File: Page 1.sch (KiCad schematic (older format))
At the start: 36 parts, among them J1 10118192-0001LF, J2 ARJM11A3, U1 AZ1117-3.3, U2 LAN8720A

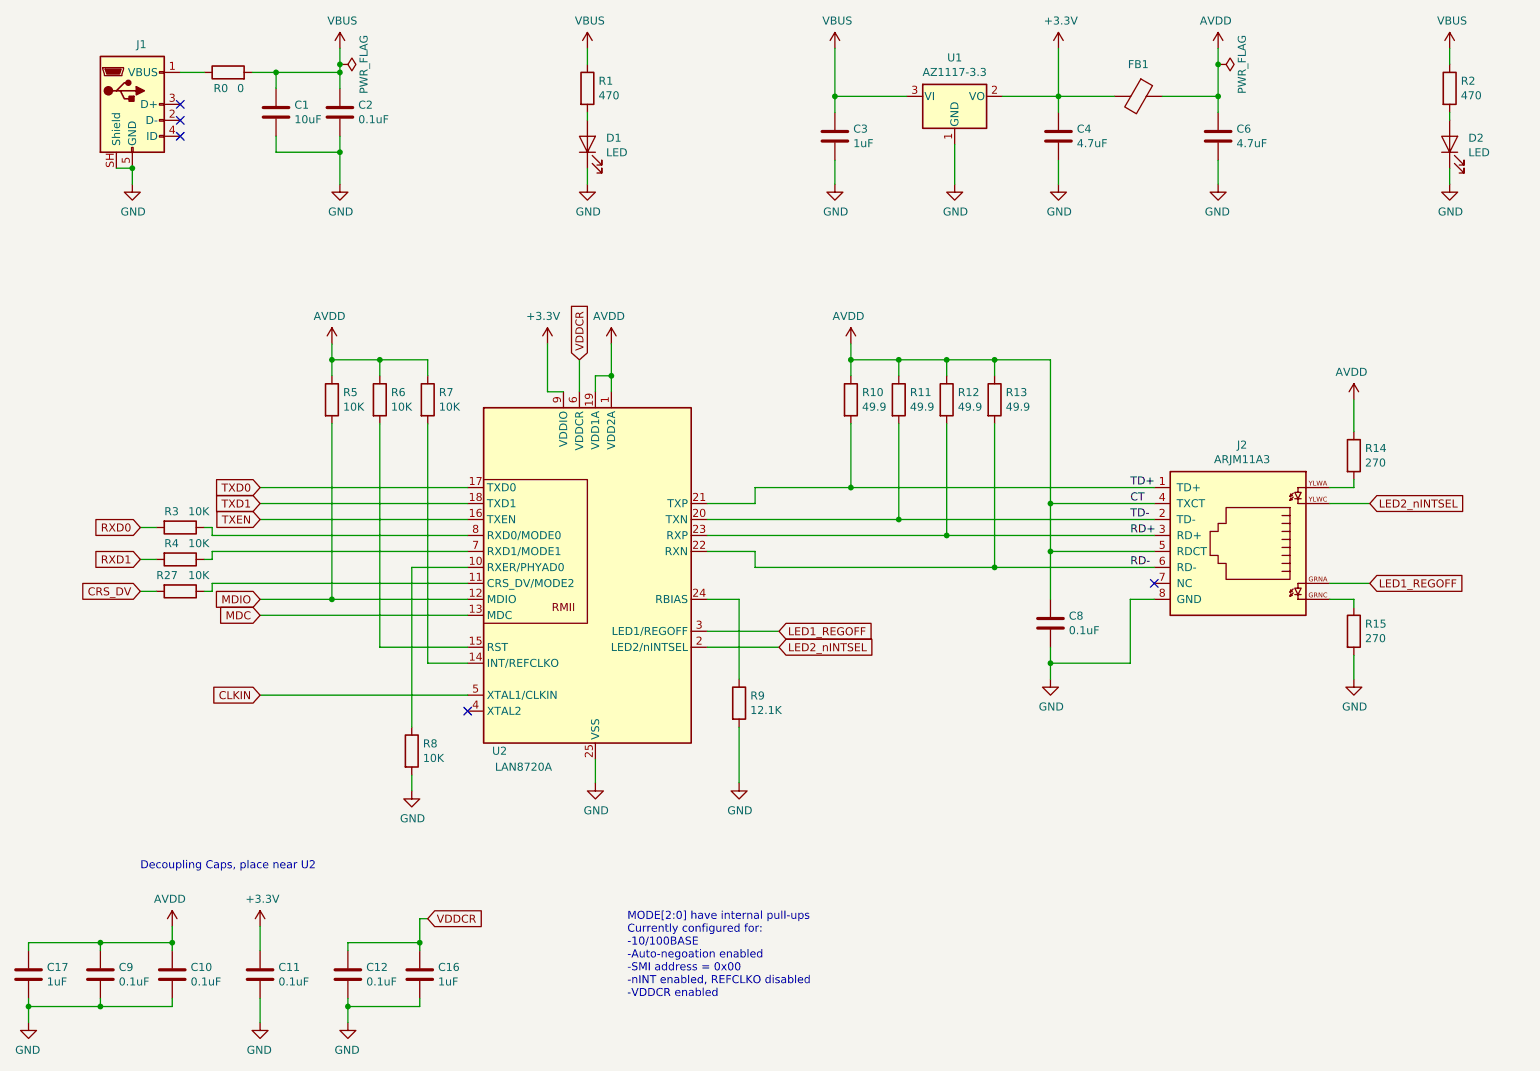
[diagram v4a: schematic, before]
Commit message: Schematic changes
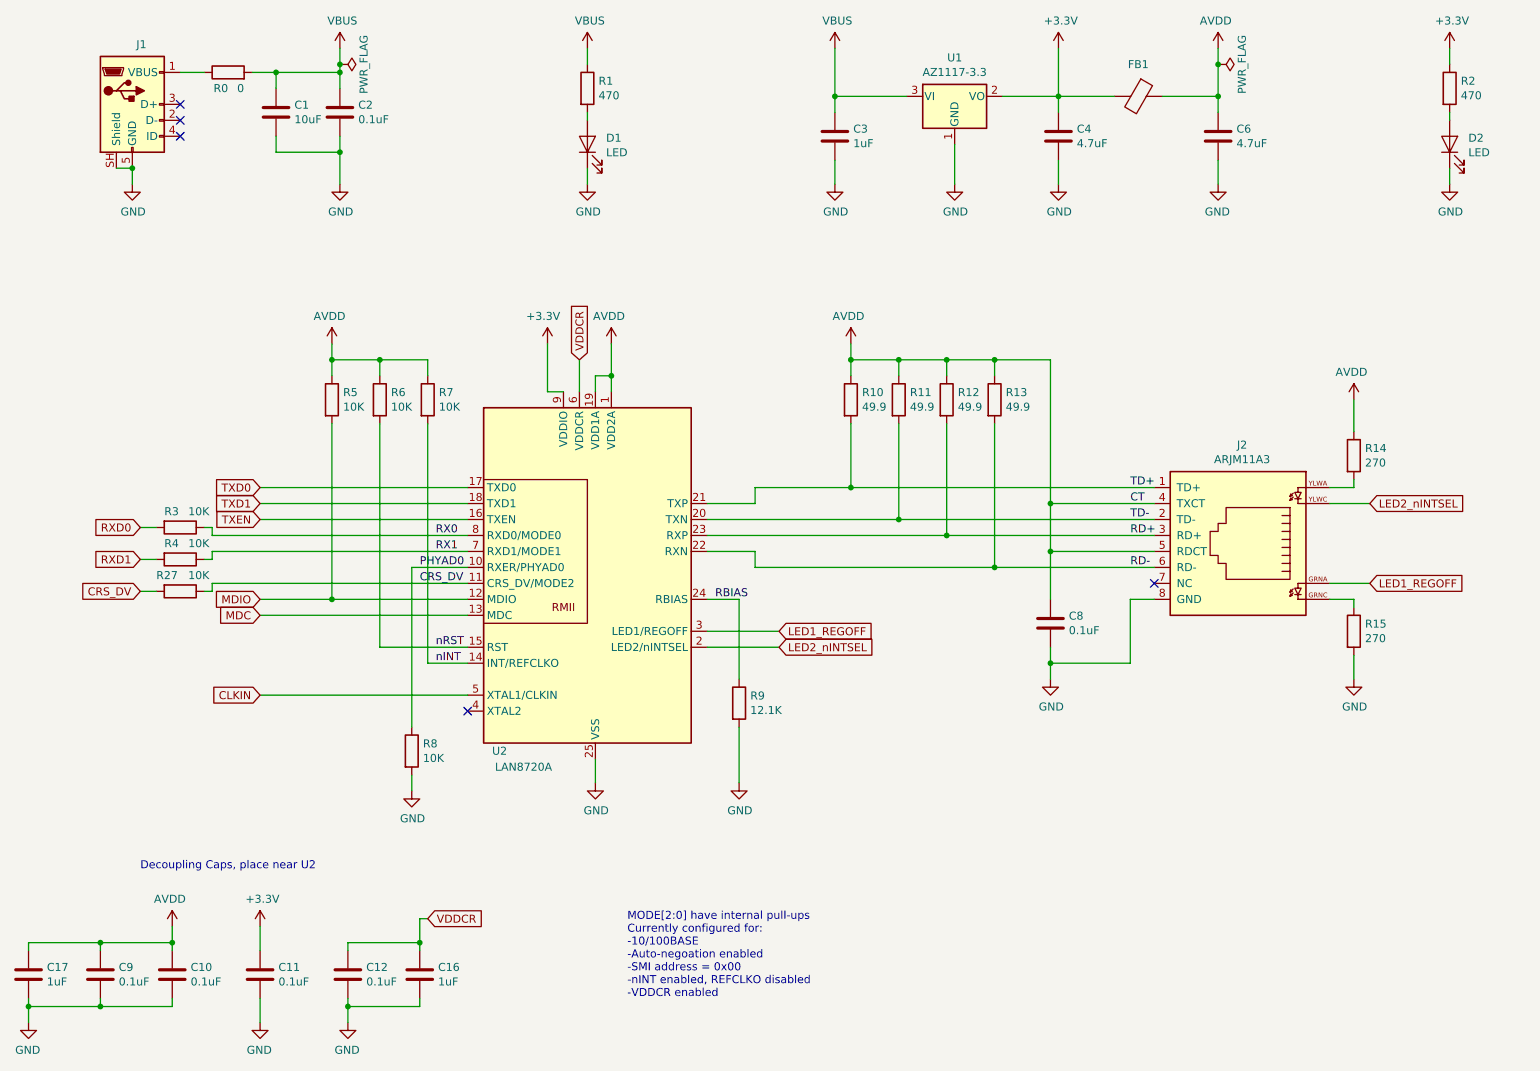
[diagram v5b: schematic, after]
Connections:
- net +3V3: now also R2.1
- net CRS_DV: now also R27.1, U2.11 (CRS_DV/MODE2)
- net VBUS: no longer R2.1
- net PHYAD0: now reaches R8.1, U2.10 (RXER/PHYAD0)
- net nINT: now reaches R7.2, U2.14 (INT/REFCLKO)
- net nRST: now reaches R6.2, U2.15 (RST)
- net RBIAS: now reaches R9.1, U2.24 (RBIAS)
- net RX1: now reaches R4.1, U2.7 (RXD1/MODE1)
- net RX0: now reaches R3.1, U2.8 (RXD0/MODE0)
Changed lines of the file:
@@
 	6150 1950 6150 2100
-$Comp
-L power:VBUS #PWR?
-U 1 1 5DF04C3D
-P 10000 1250
-AR Path="/5DF04C3D" Ref="#PWR?"  Part="1"
-AR Path="/5DED2F9B/5DF04C3D" Ref="#PWR0111"  Part="1"
-F 0 "#PWR0111" H 10000 1100 50  0001 C CNN
-F 1 "VBUS" H 10015 1423 50  0000 C CNN
-F 2 "" H 10000 1250 50  0001 C CNN
-F 3 "" H 10000 1250 50  0001 C CNN
-	1    10000 1250
-	1    0    0    -1
-$EndComp
 $Comp
 L power:GND #PWR?
@@
 Wire Wire Line
 	8550 1950 8550 2100
+Wire Wire Line
+	1800 4650 1900 4650
+Wire Wire Line
+	2200 4650 2250 4650
+Wire Wire Line
+	2250 4650 2250 4600
+Wire Wire Line
+	2250 4600 3850 4600
 $Comp
 L Device:R R?
@@
 	0    1    1    0
 $EndComp
-Wire Wire Line
-	1800 4650 1900 4650
-Wire Wire Line
-	2200 4650 2250 4650
-Wire Wire Line
-	2250 4650 2250 4600
-Wire Wire Line
-	2250 4600 3850 4600
+Text Label 3650 5000 0    50   ~ 0
+nRST
+Text Label 3650 5100 0    50   ~ 0
+nINT
+Text Label 3550 4500 0    50   ~ 0
+PHYAD0
+Text Label 5400 4700 0    50   ~ 0
+RBIAS
+Text Label 3650 4300 0    50   ~ 0
+RX0
+Text Label 3650 4400 0    50   ~ 0
+RX1
+Text Label 3550 4600 0    50   ~ 0
+CRS_DV
+$Comp
+L power:+3.3V #PWR?
+U 1 1 5E17203C
+P 10000 1250
+AR Path="/5E17203C" Ref="#PWR?"  Part="1"
+AR Path="/5DED2F9B/5E17203C" Ref="#PWR0111"  Part="1"
+F 0 "#PWR0111" H 10000 1100 50  0001 C CNN
+F 1 "+3.3V" H 10015 1423 50  0000 C CNN
+F 2 "" H 10000 1250 50  0001 C CNN
+F 3 "" H 10000 1250 50  0001 C CNN
+	1    10000 1250
+	1    0    0    -1
+$EndComp
 $EndSCHEMATC
